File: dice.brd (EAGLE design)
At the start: 53.3 x 55.9 mm, 10 parts

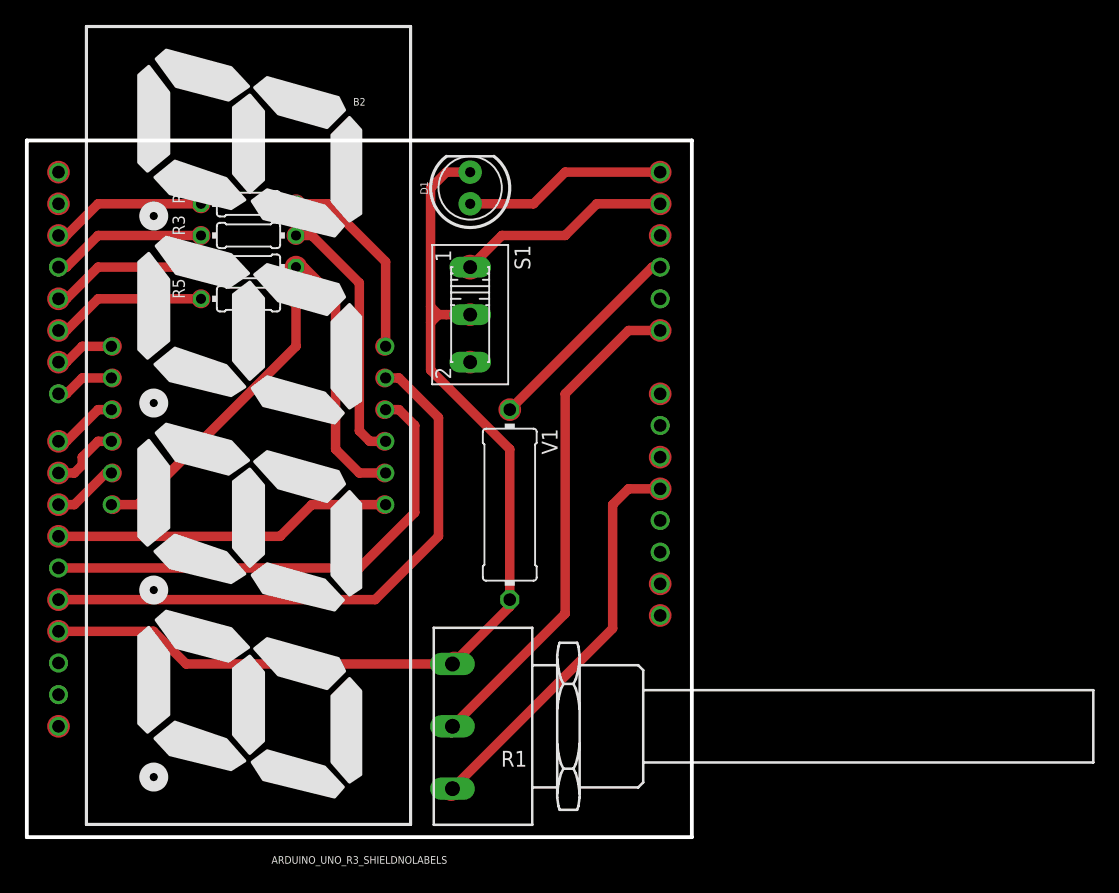
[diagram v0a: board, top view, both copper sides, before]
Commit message: Update for JLCPCB
Ground pour
Remove trace around holes
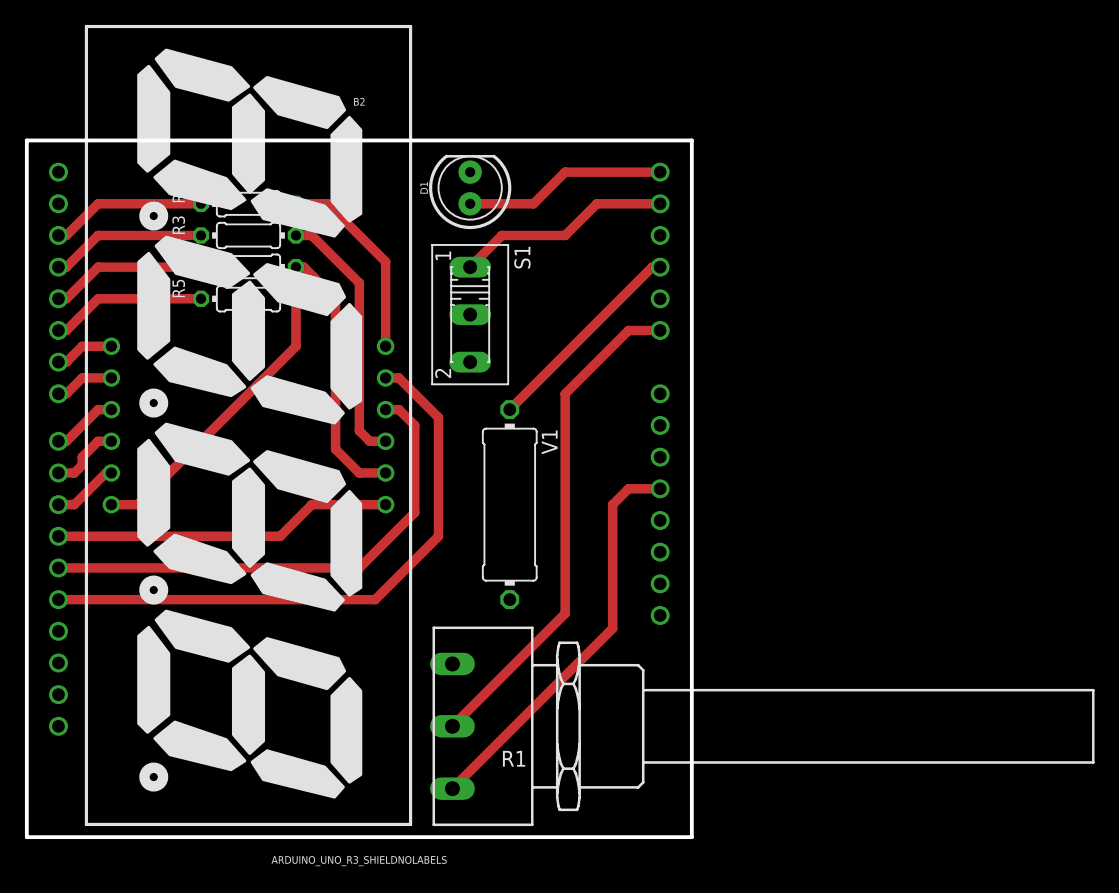
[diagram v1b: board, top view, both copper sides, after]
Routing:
- net GND: track 83.4 -> 0.00 mm
- added copper zone on layer 1, net GND
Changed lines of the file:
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@@
 <drawing>
 <settings>
-<setting alwaysvectorfont="no"/>
+<setting alwaysvectorfont="yes"/>
 <setting verticaltext="up"/>
 </settings>
@@
 <layer number="14" name="Route14" color="22" fill="1" visible="no" active="no"/>
 <layer number="15" name="Route15" color="23" fill="1" visible="no" active="no"/>
-<layer number="16" name="Bottom" color="1" fill="1" visible="yes" active="yes"/>
+<layer number="16" name="Bottom" color="1" fill="1" visible="no" active="no"/>
 <layer number="17" name="Pads" color="2" fill="1" visible="yes" active="yes"/>
 <layer number="18" name="Vias" color="2" fill="1" visible="yes" active="yes"/>
@@
 <wire x1="53.34" y1="55.88" x2="53.34" y2="0" width="0.3048" layer="20"/>
 <wire x1="0" y1="55.88" x2="53.34" y2="55.88" width="0.3048" layer="20"/>
-<circle x="2.54" y="35.56" radius="0.567959375" width="0.381" layer="1"/>
-<circle x="2.54" y="38.1" radius="0.71841875" width="0.381" layer="1"/>
-<circle x="2.54" y="40.64" radius="0.71841875" width="0.381" layer="1"/>
-<circle x="2.54" y="43.18" radius="0.71841875" width="0.381" layer="1"/>
-<circle x="2.54" y="45.72" radius="0.567959375" width="0.381" layer="1"/>
-<circle x="2.54" y="48.26" radius="0.71841875" width="0.381" layer="1"/>
-<circle x="2.54" y="50.8" radius="0.71841875" width="0.381" layer="1"/>
-<circle x="2.54" y="53.34" radius="0.71841875" width="0.381" layer="1"/>
-<circle x="6.858" y="39.37" radius="0.567959375" width="0.381" layer="1"/>
-<circle x="6.858" y="36.83" radius="0.567959375" width="0.381" layer="1"/>
-<circle x="6.858" y="34.29" radius="0.567959375" width="0.381" layer="1"/>
-<circle x="6.858" y="31.75" radius="0.567959375" width="0.381" layer="1"/>
-<circle x="2.54" y="31.75" radius="0.71841875" width="0.381" layer="1"/>
-<circle x="2.54" y="29.21" radius="0.71841875" width="0.381" layer="1"/>
-<circle x="2.54" y="26.67" radius="0.71841875" width="0.381" layer="1"/>
-<circle x="2.54" y="24.13" radius="0.71841875" width="0.381" layer="1"/>
-<circle x="2.54" y="21.59" radius="0.567959375" width="0.381" layer="1"/>
-<circle x="2.54" y="19.05" radius="0.71841875" width="0.381" layer="1"/>
-<circle x="2.54" y="16.51" radius="0.71841875" width="0.381" layer="1"/>
-<circle x="2.54" y="13.97" radius="0.567959375" width="0.381" layer="1"/>
-<circle x="2.54" y="11.43" radius="0.567959375" width="0.381" layer="1"/>
-<circle x="2.54" y="8.89" radius="0.71841875" width="0.381" layer="1"/>
-<circle x="6.858" y="29.21" radius="0.567959375" width="0.381" layer="1"/>
-<circle x="6.858" y="26.67" radius="0.567959375" width="0.381" layer="1"/>
-<circle x="13.97" y="50.8" radius="0.567959375" width="0.381" layer="1"/>
-<circle x="13.97" y="48.26" radius="0.567959375" width="0.381" layer="1"/>
-<circle x="13.97" y="45.72" radius="0.567959375" width="0.381" layer="1"/>
-<circle x="13.97" y="43.18" radius="0.567959375" width="0.381" layer="1"/>
-<circle x="21.59" y="50.8" radius="0.567959375" width="0.381" layer="1"/>
-<circle x="21.59" y="48.26" radius="0.567959375" width="0.381" layer="1"/>
-<circle x="21.59" y="45.72" radius="0.71841875" width="0.381" layer="1"/>
-<circle x="21.59" y="43.18" radius="0.567959375" width="0.381" layer="1"/>
-<circle x="28.702" y="39.37" radius="0.567959375" width="0.381" layer="1"/>
-<circle x="28.702" y="36.83" radius="0.567959375" width="0.381" layer="1"/>
-<circle x="28.702" y="34.29" radius="0.567959375" width="0.381" layer="1"/>
-<circle x="28.702" y="31.75" radius="0.567959375" width="0.381" layer="1"/>
-<circle x="28.702" y="29.21" radius="0.567959375" width="0.381" layer="1"/>
-<circle x="28.702" y="26.67" radius="0.567959375" width="0.381" layer="1"/>
-<circle x="35.56" y="53.34" radius="0.71841875" width="0.381" layer="1"/>
-<circle x="35.56" y="50.8" radius="0.71841875" width="0.381" layer="1"/>
-<circle x="35.56" y="45.72" radius="0.803215625" width="0.381" layer="1"/>
-<circle x="35.56" y="41.91" radius="0.71841875" width="0.381" layer="1"/>
-<circle x="35.56" y="38.1" radius="0.71841875" width="0.381" layer="1"/>
-<circle x="38.735" y="34.29" radius="0.71841875" width="0.381" layer="1"/>
-<circle x="38.735" y="19.05" radius="0.567959375" width="0.381" layer="1"/>
-<circle x="34.29" y="13.97" radius="0.71841875" width="0.381" layer="1"/>
-<circle x="34.036" y="8.89" radius="0.71841875" width="0.381" layer="1"/>
-<circle x="34.036" y="3.81" radius="0.71841875" width="0.381" layer="1"/>
-<circle x="50.8" y="53.34" radius="0.71841875" width="0.381" layer="1"/>
-<circle x="50.8" y="50.8" radius="0.71841875" width="0.381" layer="1"/>
-<circle x="50.8" y="48.26" radius="0.71841875" width="0.381" layer="1"/>
-<circle x="50.8" y="45.72" radius="0.567959375" width="0.381" layer="1"/>
-<circle x="50.8" y="43.18" radius="0.567959375" width="0.381" layer="1"/>
-<circle x="50.8" y="40.64" radius="0.71841875" width="0.381" layer="1"/>
-<circle x="50.8" y="35.56" radius="0.71841875" width="0.381" layer="1"/>
-<circle x="50.8" y="33.02" radius="0.567959375" width="0.381" layer="1"/>
-<circle x="50.8" y="30.48" radius="0.71841875" width="0.381" layer="1"/>
-<circle x="50.8" y="27.94" radius="0.71841875" width="0.381" layer="1"/>
-<circle x="50.8" y="25.4" radius="0.567959375" width="0.381" layer="1"/>
-<circle x="50.8" y="22.86" radius="0.567959375" width="0.381" layer="1"/>
-<circle x="50.8" y="20.32" radius="0.71841875" width="0.381" layer="1"/>
-<circle x="50.8" y="17.78" radius="0.71841875" width="0.381" layer="1"/>
 </plain>
 <attributes>
@@
 necessary adjustments and save your customized
 design rules under a new name.</description>
-<param name="layerSetup" value="(1*16)"/>
+<param name="layerSetup" value="1"/>
 <param name="mtCopper" value="0.035mm 0.035mm 0.035mm 0.035mm 0.035mm 0.035mm 0.035mm 0.035mm 0.035mm 0.035mm 0.035mm 0.035mm 0.035mm 0.035mm 0.035mm 0.035mm"/>
 <param name="mtIsolate" value="1.5mm 0.15mm 0.2mm 0.15mm 0.2mm 0.15mm 0.2mm 0.15mm 0.2mm 0.15mm 0.2mm 0.15mm 0.2mm 0.15mm 0.2mm"/>
@@
 <contactref element="V1" pad="2"/>
 <contactref element="B2" pad="GND@2"/>
-<wire x1="2.54" y1="16.51" x2="10.16" y2="16.51" width="0.762" layer="1"/>
-<wire x1="10.16" y1="16.51" x2="12.78" y2="13.89" width="0.762" layer="1"/>
-<wire x1="12.78" y1="13.89" x2="34.14" y2="13.89" width="0.762" layer="1"/>
-<wire x1="38.735" y1="19.05" x2="38.735" y2="18.485" width="0.762" layer="1"/>
-<wire x1="38.735" y1="18.485" x2="34.14" y2="13.89" width="0.762" layer="1"/>
-<wire x1="38.735" y1="31.115" x2="38.735" y2="19.05" width="0.762" layer="1"/>
-<wire x1="33.02" y1="41.91" x2="32.385" y2="41.275" width="0.762" layer="1"/>
-<wire x1="38.735" y1="31.115" x2="32.385" y2="37.465" width="0.762" layer="1"/>
-<wire x1="32.385" y1="37.465" x2="32.385" y2="41.275" width="0.762" layer="1"/>
-<wire x1="35.56" y1="41.91" x2="33.655" y2="41.91" width="0.762" layer="1"/>
-<wire x1="32.385" y1="52.07" x2="32.385" y2="42.545" width="0.762" layer="1"/>
-<wire x1="32.385" y1="42.545" x2="32.385" y2="41.275" width="0.762" layer="1"/>
-<wire x1="35.56" y1="53.34" x2="33.655" y2="53.34" width="0.762" layer="1"/>
-<wire x1="33.655" y1="53.34" x2="32.385" y2="52.07" width="0.762" layer="1"/>
-<wire x1="33.655" y1="41.91" x2="33.02" y2="41.91" width="0.762" layer="1"/>
-<wire x1="33.02" y1="41.91" x2="32.385" y2="42.545" width="0.762" layer="1"/>
+<polygon width="0.1524" layer="1">
+<vertex x="0" y="55.88"/>
+<vertex x="53.34" y="55.88"/>
+<vertex x="53.34" y="0"/>
+<vertex x="0" y="0"/>
+</polygon>
 </signal>
 <signal name="SW">
@@
 <mfgpreviewcolor name="substratecolor" color="0xFF786E46"/>
 </mfgpreviewcolors>
-<errors>
-</errors>
 </board>
 </drawing>
